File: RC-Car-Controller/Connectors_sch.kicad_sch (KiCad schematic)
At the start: 9 parts, among them J1 Conn_01x02, J2 2171790001, J3 MCU_IF, J4 RF_IF, J5 ANT_IF, U1 USBLC6-2SC6

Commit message: most resistors given PNs
most resistors given PNs. some remaining
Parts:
- R4, R5: MANUF_PN (none) -> CRCW06035K11FKEAC
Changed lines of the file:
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@@
+			)
+		)
+		(property "MANUF_PN" ""
+			(at 121.92 78.74 0)
+			(effects
+				(font
+					(size 1.27 1.27)
+				)
+				(hide yes)
 			)
 		)
@@
 			)
 		)
+		(property "MANUF_PN" ""
+			(at 128.27 137.16 0)
+			(effects
+				(font
+					(size 1.27 1.27)
+				)
+				(hide yes)
+			)
+		)
 		(pin "5"
 		)
@@
 			)
 		)
+		(property "MANUF_PN" "CRCW06035K11FKEAC"
+			(at 104.14 92.71 0)
+			(effects
+				(font
+					(size 1.27 1.27)
+				)
+				(hide yes)
+			)
+		)
 		(pin "1"
 		)
@@
 			)
 		)
+		(property "MANUF_PN" ""
+			(at 104.14 83.82 0)
+			(effects
+				(font
+					(size 1.27 1.27)
+				)
+				(hide yes)
+			)
+		)
 		(pin "A4/B9"
 		)
@@
 			)
 		)
+		(property "MANUF_PN" ""
+			(at 128.27 160.02 0)
+			(effects
+				(font
+					(size 1.27 1.27)
+				)
+				(hide yes)
+			)
+		)
 		(pin "5"
 		)
@@
 			)
 		)
+		(property "MANUF_PN" ""
+			(at 62.23 152.4 0)
+			(effects
+				(font
+					(size 1.27 1.27)
+				)
+				(hide yes)
+			)
+		)
 		(pin "1"
 		)
@@
 			)
 		)
+		(property "MANUF_PN" ""
+			(at 60.96 129.54 0)
+			(effects
+				(font
+					(size 1.27 1.27)
+				)
+				(hide yes)
+			)
+		)
 		(pin "1"
 		)
@@
 			)
 		)
+		(property "MANUF_PN" "CRCW06035K11FKEAC"
+			(at 106.68 92.71 0)
+			(effects
+				(font
+					(size 1.27 1.27)
+				)
+				(hide yes)
+			)
+		)
 		(pin "1"
 		)
@@
 			(at 179.07 135.89 0)
 			(effects
+				(font
+					(size 1.27 1.27)
+				)
+				(hide yes)
+			)
+		)
+		(property "MANUF_PN" ""
+			(at 179.07 135.89 0)
+			(effects

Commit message: controller cpnts given MANUF_PNs
controller cpnts given MANUF_PNs. not all components, but all resistors are done
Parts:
- J2: MANUF_PN (none) -> 2171790001
- S1: MANUF_PN (none) -> R1966ABLKBLKGR
- U1: MANUF_PN (none) -> USBLC6-2SC6
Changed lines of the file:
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@@
 			)
 		)
-		(property "MANUF_PN" ""
+		(property "MANUF_PN" "USBLC6-2SC6"
 			(at 121.92 78.74 0)
 			(effects
@@
 			)
 		)
-		(property "MANUF_PN" ""
+		(property "MANUF_PN" "2171790001"
 			(at 104.14 83.82 0)
 			(effects
@@
 			)
 		)
-		(property "MANUF_PN" ""
+		(property "MANUF_PN" "R1966ABLKBLKGR"
 			(at 62.23 152.4 0)
 			(effects

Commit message: Filled out some Controller Caps
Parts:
- J1: MANUF_PN (none) -> B2B-XH-AM
- J3, J4: MANUF_PN (none) -> PH2-08-UA
- J5: MANUF_PN (none) -> 0732511153
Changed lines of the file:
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@@
 			)
 		)
-		(property "MANUF_PN" ""
+		(property "MANUF_PN" "PH2-08-UA"
 			(at 128.27 137.16 0)
 			(effects
@@
 			)
 		)
-		(property "MANUF_PN" ""
+		(property "MANUF_PN" "PH2-08-UA"
 			(at 128.27 160.02 0)
 			(effects
@@
 			)
 		)
-		(property "MANUF_PN" ""
+		(property "MANUF_PN" "B2B-XH-AM"
 			(at 60.96 129.54 0)
 			(effects
@@
 			)
 		)
-		(property "MANUF_PN" ""
+		(property "MANUF_PN" "0732511153"
 			(at 179.07 135.89 0)
 			(effects

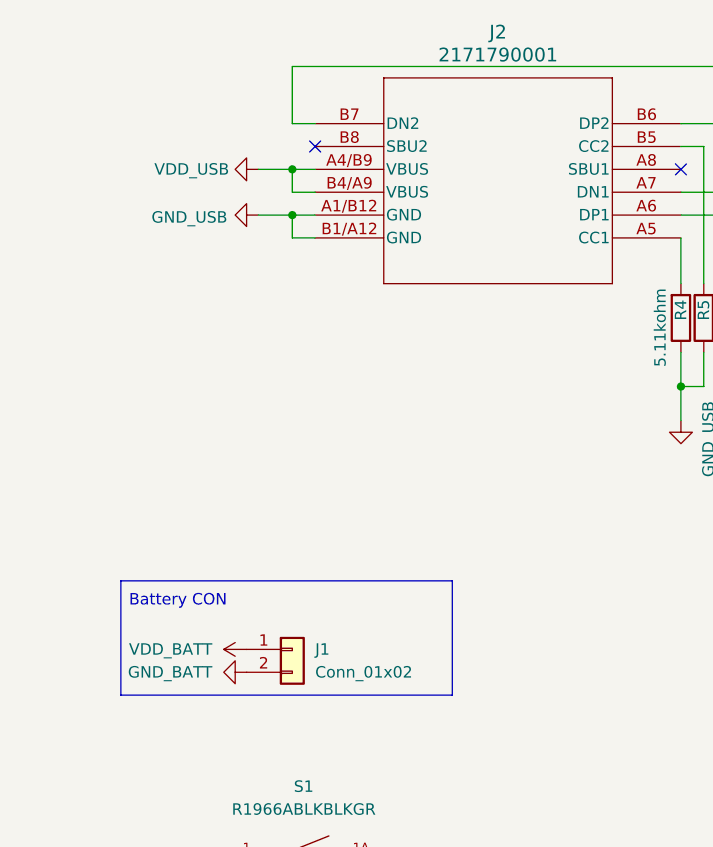
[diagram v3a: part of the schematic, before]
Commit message: Finished BOM Drafts
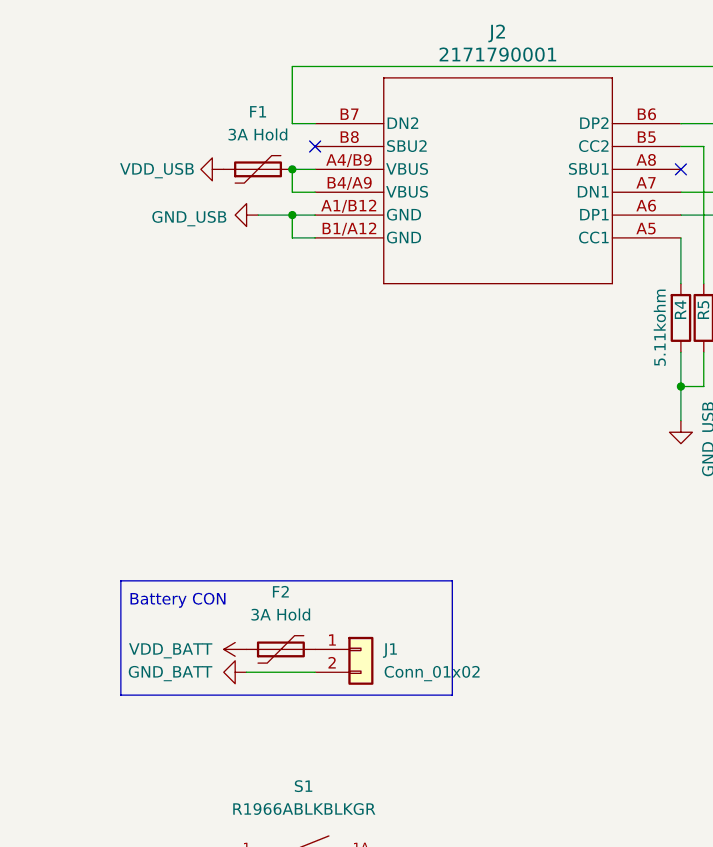
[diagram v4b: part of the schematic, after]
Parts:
- added F1, F2: 3A Hold, Fuse:Fuse_1812_4532Metric_Pad1.30x3.40mm_HandSolder, symbol Device:Polyfuse
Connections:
- net VDD_BATT: now also F2.1; no longer J1.1 (Pin_1)
- net VDD_USB: now also F1.1; no longer J2.A4/B9 (VBUS), J2.B4/A9 (VBUS)
- new net: F1.2, J2.A4/B9 (VBUS), J2.B4/A9 (VBUS)
- new net: F2.2, J1.1 (Pin_1)
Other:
- moved on the sheet: J1
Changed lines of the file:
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@@
+	(wire
+		(pts
+			(xy 63.5 132.08) (xy 55.88 132.08)
+		)
+		(stroke
+			(width 0)
+			(type default)
+		)
+	)
 	(wire
 		(pts
@@
 		(pts
 			(xy 109.22 64.77) (xy 60.96 64.77)
-		)
-		(stroke
-			(width 0)
-			(type default)
-		)
-	)
-	(wire
-		(pts
-			(xy 57.15 76.2) (xy 60.96 76.2)
 		)
 		(stroke
@@
 	)
 	(symbol
+		(lib_id "Device:Polyfuse")
+		(at 57.15 76.2 90)
+		(unit 1)
+		(exclude_from_sim no)
+		(in_bom yes)
+		(on_board yes)
+		(dnp no)
+		(fields_autoplaced yes)
+		(property "Reference" "F1"
+			(at 57.15 69.85 90)
+			(effects
+				(font
+					(size 1.27 1.27)
+				)
+			)
+		)
+		(property "Value" "3A Hold"
+			(at 57.15 72.39 90)
+			(effects
+				(font
+					(size 1.27 1.27)
+				)
+			)
+		)
+		(property "Footprint" "Fuse:Fuse_1812_4532Metric_Pad1.30x3.40mm_HandSolder"
+			(at 62.23 74.93 0)
+			(effects
+				(font
+					(size 1.27 1.27)
+				)
+				(justify left)
+				(hide yes)
+			)
+		)
+		(property "Datasheet" "~"
+			(at 57.15 76.2 0)
+			(effects
+				(font
+					(size 1.27 1.27)
+				)
+				(hide yes)
+			)
+		)
+		(property "Description" "Resettable fuse, polymeric positive temperature coefficient"
+			(at 57.15 76.2 0)
+			(effects
+				(font
+					(size 1.27 1.27)
+				)
+				(hide yes)
+			)
+		)
+		(property "MANUF_PN" "0ZCG0300FF2B"
+			(at 57.15 76.2 0)
+			(effects
+				(font
+					(size 1.27 1.27)
+				)
+				(hide yes)
+			)
+		)
+		(pin "1"
+		)
+		(pin "2"
+		)
+		(instances
+			(project "RC-Car-Controller"
+				(path "/ba870fd1-751d-4755-8e1a-1ea86ca9e2f6/47812da9-b622-4bda-8507-4e09448e1ff5"
+					(reference "F1")
+					(unit 1)
+				)
+			)
+		)
+	)
+	(symbol
 		(lib_id "power:+3V3")
 		(at 69.85 152.4 270)
@@
 	(symbol
 		(lib_id "Connector_Generic:Conn_01x02")
-		(at 60.96 129.54 0)
+		(at 68.58 129.54 0)
 		(unit 1)
 		(exclude_from_sim no)
@@
 		(fields_autoplaced yes)
 		(property "Reference" "J1"
-			(at 63.5 129.5399 0)
+			(at 71.12 129.5399 0)
 			(effects
 				(font
@@
 		)
 		(property "Value" "Conn_01x02"
-			(at 63.5 132.0799 0)
+			(at 71.12 132.0799 0)
 			(effects
 				(font
@@
 		)
 		(property "Footprint" "Connector_JST:JST_XH_B2B-XH-AM_1x02_P2.50mm_Vertical"
-			(at 60.96 129.54 0)
+			(at 68.58 129.54 0)
 			(effects
 				(font
@@
 		)
 		(property "Datasheet" "~"
-			(at 60.96 129.54 0)
+			(at 68.58 129.54 0)
 			(effects
 				(font
@@
 		)
 		(property "Description" "Generic connector, single row, 01x02, script generated (kicad-library-utils/schlib/autogen/connector/)"
-			(at 60.96 129.54 0)
+			(at 68.58 129.54 0)
 			(effects
 				(font
@@
 		)
 		(property "MANUF_PN" "B2B-XH-AM"
-			(at 60.96 129.54 0)
+			(at 68.58 129.54 0)
 			(effects
 				(font
@@
 	)
 	(symbol
+		(lib_id "Device:Polyfuse")
+		(at 59.69 129.54 90)
+		(unit 1)
+		(exclude_from_sim no)
+		(in_bom yes)
+		(on_board yes)
+		(dnp no)
+		(fields_autoplaced yes)
+		(property "Reference" "F2"
+			(at 59.69 123.19 90)
+			(effects
+				(font
+					(size 1.27 1.27)
+				)
+			)
+		)
+		(property "Value" "3A Hold"
+			(at 59.69 125.73 90)
+			(effects
+				(font
+					(size 1.27 1.27)
+				)
+			)
+		)
+		(property "Footprint" "Fuse:Fuse_1812_4532Metric_Pad1.30x3.40mm_HandSolder"
+			(at 64.77 128.27 0)
+			(effects
+				(font
+					(size 1.27 1.27)
+				)
+				(justify left)
+				(hide yes)
+			)
+		)
+		(property "Datasheet" "~"
+			(at 59.69 129.54 0)
+			(effects
+				(font
+					(size 1.27 1.27)
+				)
+				(hide yes)
+			)
+		)
+		(property "Description" "Resettable fuse, polymeric positive temperature coefficient"
+			(at 59.69 129.54 0)
+			(effects
+				(font
+					(size 1.27 1.27)
+				)
+				(hide yes)
+			)
+		)
+		(property "MANUF_PN" "0ZCG0300FF2B"
+			(at 59.69 129.54 0)
+			(effects
+				(font
+					(size 1.27 1.27)
+				)
+				(hide yes)
+			)
+		)
+		(pin "1"
+		)
+		(pin "2"
+		)
+		(instances
+			(project "RC-Car-Controller"
+				(path "/ba870fd1-751d-4755-8e1a-1ea86ca9e2f6/47812da9-b622-4bda-8507-4e09448e1ff5"
+					(reference "F2")
+					(unit 1)
+				)
+			)
+		)
+	)
+	(symbol
 		(lib_id "power:GND")
-		(at 57.15 76.2 270)
+		(at 53.34 76.2 270)
 		(unit 1)
 		(exclude_from_sim no)
@@
 		(dnp no)
 		(property "Reference" "#PWR025"
-			(at 50.8 76.2 0)
+			(at 46.99 76.2 0)
 			(effects
 				(font
@@
 		)
 		(property "Value" "VDD_USB"
-			(at 49.784 76.2 90)
+			(at 45.974 76.2 90)
 			(effects
 				(font
@@
 		)
 		(property "Footprint" ""
-			(at 57.15 76.2 0)
+			(at 53.34 76.2 0)
 			(effects
 				(font
@@
 		)
 		(property "Datasheet" ""
-			(at 57.15 76.2 0)
+			(at 53.34 76.2 0)
 			(effects
 				(font
@@
 		)
 		(property "Description" "Power symbol creates a global label with name \"GND\" , ground"
-			(at 57.15 76.2 0)
-			(effects
-				(font
+			(at 53.34 76.2 0)
+			(effects
+				(font
